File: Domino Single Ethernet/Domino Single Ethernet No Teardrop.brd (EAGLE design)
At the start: 45.7 x 33 mm, 42 parts, among them J1 11A009-1702-00, J2 MH18-1, J3 MH18-1

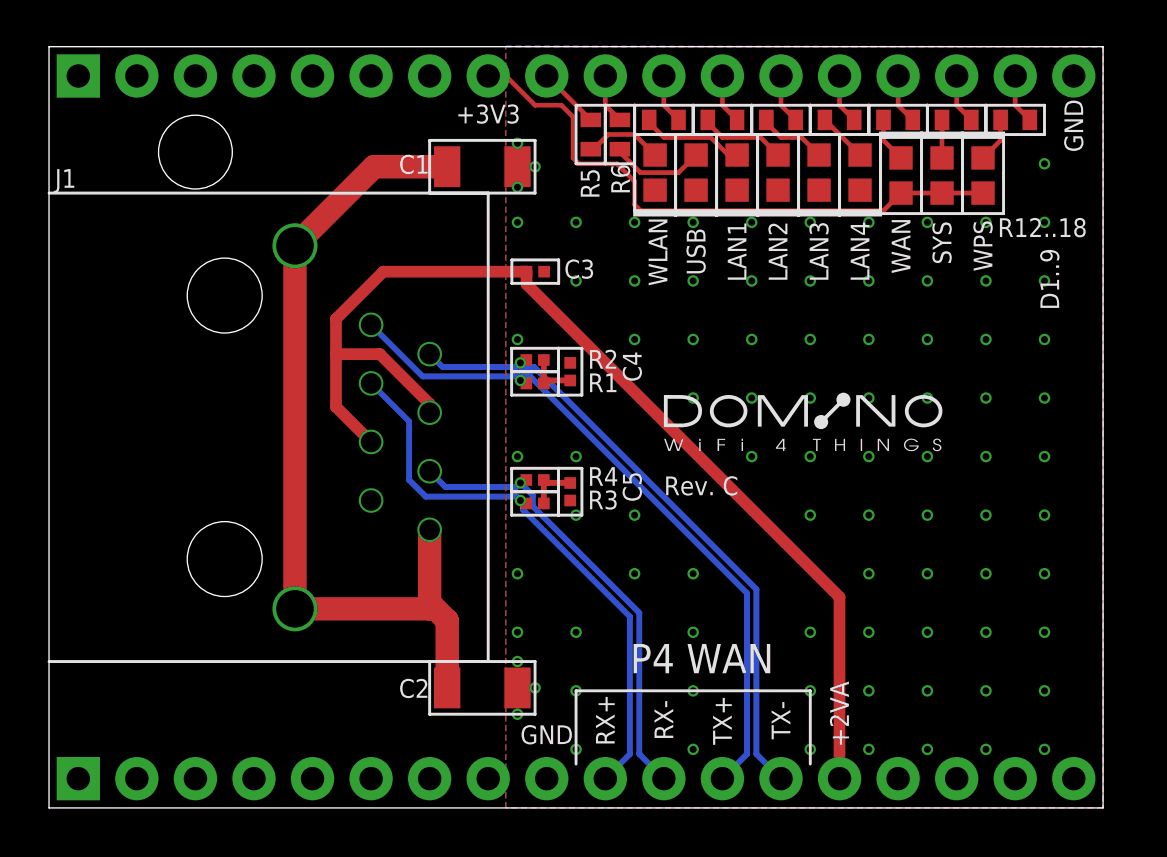
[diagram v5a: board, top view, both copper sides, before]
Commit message: Domnio Single Ethernet Rev. D: changed silkscreen font ratio to 20%
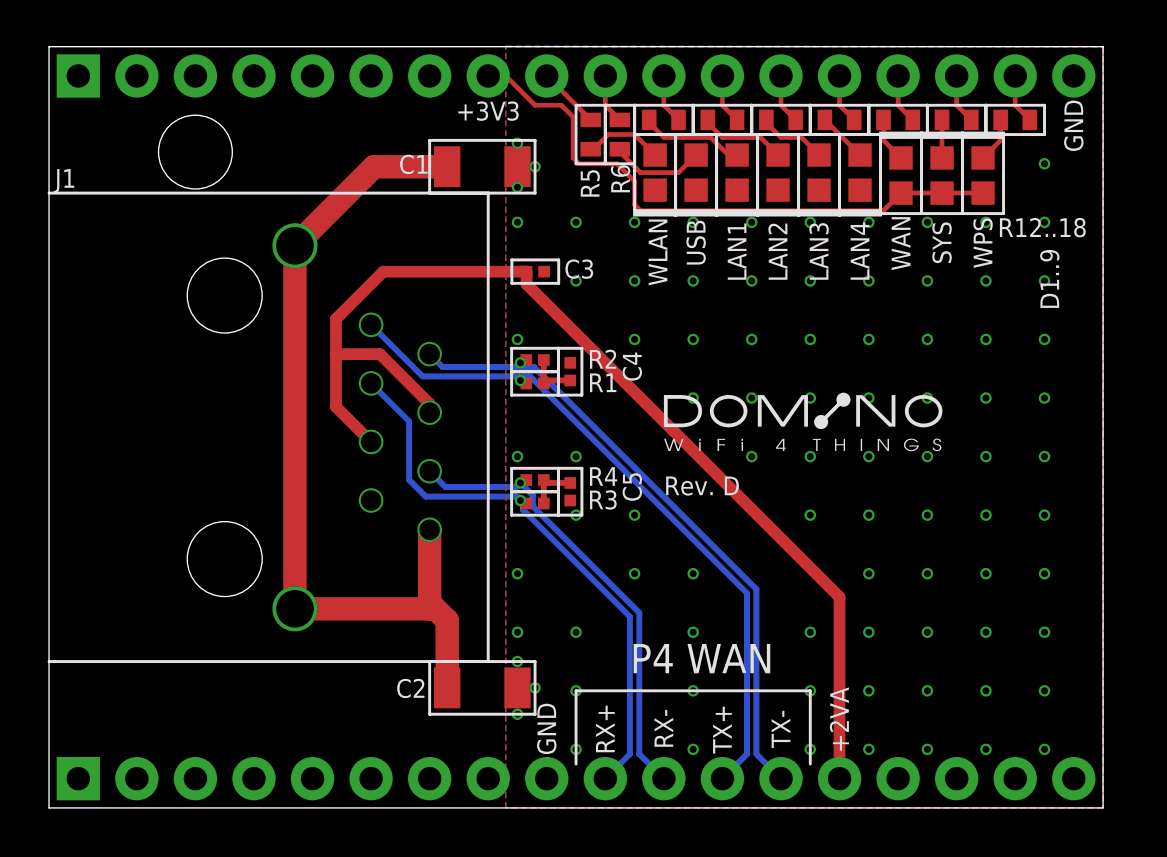
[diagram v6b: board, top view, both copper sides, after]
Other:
- board text added: "© 2014-2015, The Domino Team. All rights reserved."
- board text removed: "© 2014, The Domino Team. All rights reserved."

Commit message: Added UART header to both Ethernet tiles
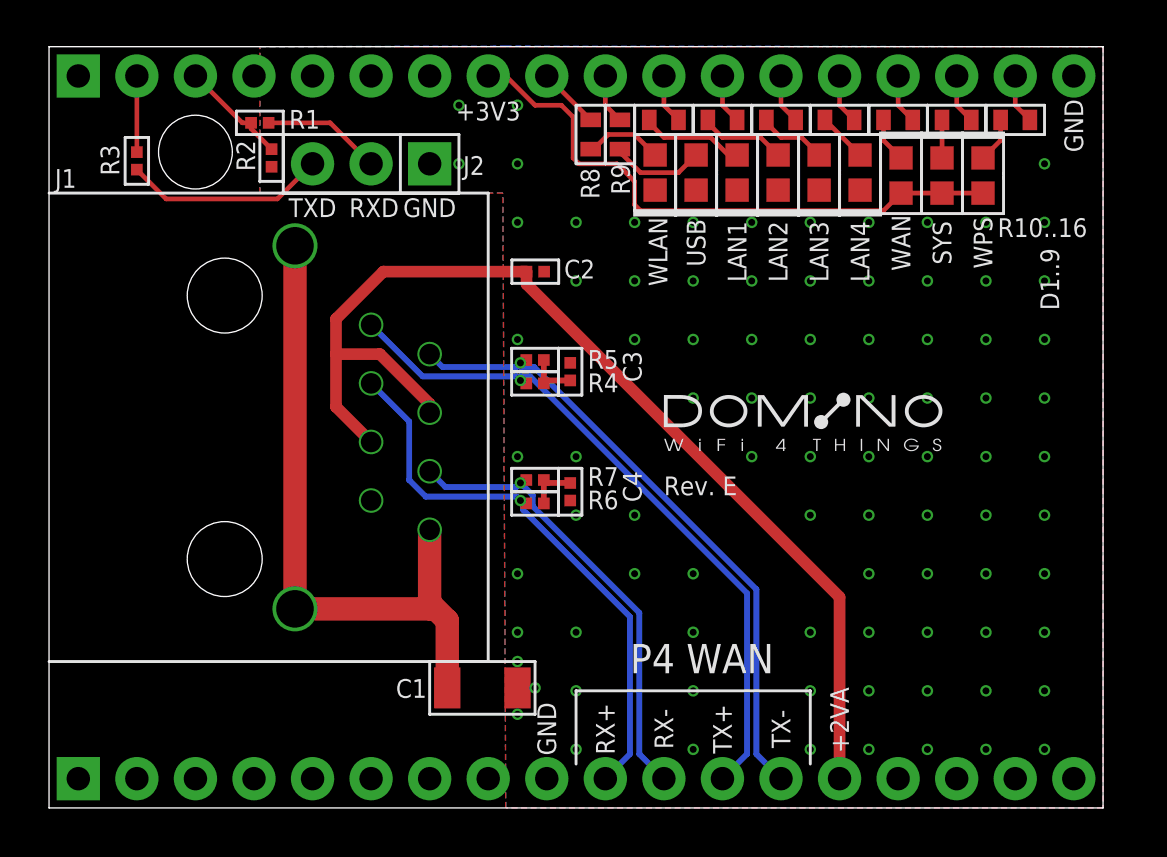
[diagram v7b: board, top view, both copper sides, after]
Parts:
- removed C5: 100n, Domino:C0402
- added J4: MH18-1, Domino:MH18-1-0.1
- added R14, R15, R16: 330R, Domino:R0603
- C2: value 2n2 -> 100n; device Domino:C1206 -> Domino:C0402
- J2: value MH18-1 -> MH3-1; device Domino:MH18-1-0.1 -> Domino:MH3-1-0.1
- R1: value 49R9 -> 4k7
- R11, R12, R13: value 330R -> 270R
- R2: value 49R9 -> 15k
- R3: value 49R9 -> 220R
- R5, R6, R7: value 270R -> 49R9; device Domino:R0603 -> Domino:R0402
- moved J3 30.5 mm to (1.27, 31.8)
- moved R3 22.8 mm to (3.81, 28.1), turned to 90 degrees
- moved C1 22.6 mm to (18.8, 5.21)
- moved C2 18.2 mm to (21.1, 23.3)
- moved R7 16.6 mm to (21.1, 14.2)
- moved R1 16.4 mm to (9.14, 29.7)
- moved R6 16.4 mm to (21.1, 13.2), turned to 180 degrees
- moved R2 14.4 mm to (9.65, 28.2), turned to 270 degrees
- moved J2 13.3 mm to (14.0, 27.9), flipped to the top
- moved R5 10.1 mm to (21.1, 19.4), turned to 180 degrees
- moved R10 7.62 mm to (26.7, 29.8)
- moved R11 7.62 mm to (29.2, 29.8)
- moved R12 7.62 mm to (31.8, 29.8)
- moved R13 7.62 mm to (34.3, 29.8)
- moved R9 7.01 mm to (24.8, 29.2), turned to 270 degrees
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- renumbered U$10 to L1
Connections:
- new net RXD: J2.2, R1.1
- new net TXD: J2.3, R3.1
- new net UART_RX: J3.3, R1.2, R2.1
- new net UART_TX: J3.2, R3.2
- net +2VA_ETH_OUT: now also C2.2, J4.14; no longer C3.2, J3.14
- net +3V3: now also J3.8; no longer J2.8
- net GND: now also J2.1, J3.18, J3.6, J4.9, R2.2; no longer C5.1, J2.18, J3.9
- net LAN1_LED: now also R10.2; no longer R7.2
- net LAN2_LED: now also R11.2; no longer R8.2
- net LAN3_LED: now also R12.2; no longer R9.2
- net LAN4_LED: now also R13.2; no longer R10.2
- net LED0: now also J3.9, R8.1; no longer J2.9, R5.1
- net LED1: now also J3.10, R9.1; no longer J2.10, R6.1
- net LED2: now also J3.11, R10.1; no longer J2.11, R7.1
- net LED3: now also J3.12, R11.1; no longer J2.12, R8.1
- net LED4: now also J3.13, R12.1; no longer J2.13, R9.1
- net LED5: now also J3.14, R13.1; no longer J2.14, R10.1
- net LED6: now also J3.15, R14.1; no longer J2.15, R11.1
- net LED7: now also J3.16, R15.1; no longer J2.16, R12.1
- net LED8: now also J3.17, R16.1; no longer J2.17, R13.1
- net P4_RX: now also C4.2, R6.1, R7.1; no longer C5.2, R3.1, R4.1
- net P4_RX_N: now also J4.11, R7.2; no longer J3.11, R4.2
- net P4_RX_P: now also J4.10, R6.2; no longer J3.10, R3.2
- net P4_TX: now also C3.2, R4.1, R5.1; no longer C4.2, R1.1, R2.1
- net P4_TX_N: now also J4.13, R5.2; no longer J3.13, R2.2
- net P4_TX_P: now also J4.12, R4.2; no longer J3.12, R1.2
- net SHIELD: no longer C2.2
- net SYS_LED: now also R15.2; no longer R12.2
- net USB_LED: now also R9.2; no longer R6.2
- net WAN_LED: now also R14.2; no longer R11.2
- net WLAN_LED: now also R8.2; no longer R5.2
- net WPS_LED: now also R16.2; no longer R13.2
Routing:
- net TXD: track 0.00 -> 8.78 mm
- net SHIELD: track 37.0 -> 29.0 mm
- net RXD: track 0.00 -> 5.18 mm
- net UART_RX: track 0.00 -> 4.77 mm
- net UART_TX: track 0.00 -> 3.30 mm
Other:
- board text added: "R10..16"
- board text added: "RXD"
- board text added: "TXD"
- board text added: "UART_RX"
- board text added: "UART_TX"
- board text removed: "R12..18"
